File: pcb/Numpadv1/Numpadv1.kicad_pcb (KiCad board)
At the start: 2 copper layers, 104.8 x 100 mm, 37 parts, among them J1 OLED_128x32, SW1 RotaryEncoder_Switch, U1 RP2040_Zero

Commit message: PCB Completed (for now)
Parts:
- added H1: ~, ScottoKeebs_Scotto:Standoff_M2x4mm, B.Cu at (83.2, 67.3)
- added H2: ~, ScottoKeebs_Scotto:Standoff_M2x4mm, B.Cu at (83.2, 124.5)
- added H3: ~, ScottoKeebs_Scotto:Standoff_M2x4mm, B.Cu at (140.3, 105.4)
- added SW2: Switch, ScottoKeebs_Stabilizer:Stabilizer_MX_2.00u, F.Cu at (83.2, 134.0)
- added SW3: Switch, ScottoKeebs_Stabilizer:Stabilizer_MX_2.00u, F.Cu at (130.8, 124.5)
- added SW4: Switch, ScottoKeebs_Stabilizer:Stabilizer_MX_2.00u, F.Cu at (130.8, 86.4)
- S1, S10, S11, S12, S13, S14, S15, S2, S3, S4, S6, S7, S8, S9: footprint ScottoKeebs_MX:MX_PCB_1.00u -> ScottoKeebs_Hotswap:Hotswap_MX_1.00u
- S16, S17: footprint Button_Switch_Keyboard:SW_Cherry_MX_2.00u_Vertical_PCB -> ScottoKeebs_Hotswap:Hotswap_MX_2.00u_90deg
- S5: footprint Button_Switch_Keyboard:SW_Cherry_MX_2.00u_PCB -> ScottoKeebs_Hotswap:Hotswap_MX_2.00u
- moved SW1 45.1 mm to (153.5, 85.0)
- moved J1 21.4 mm to (159.4, 99.0)
- moved D13 8.57 mm to (121.3, 109.2)
- moved D11 8.57 mm to (121.3, 71.1)
- moved S5 5.68 mm to (83.2, 134.0)
- moved S16 5.68 mm to (130.8, 86.4)
- moved S17 5.68 mm to (130.8, 124.5)
- moved D12 3.81 mm to (121.3, 94.9)
- moved D14 3.81 mm to (121.3, 133.0)
- moved U1 1.91 mm to (154.1, 60.2)
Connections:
- D16 pad 1: /Row 1 -> /Row 2
- D17 pad 1: /Row 3 -> /Row 4
- S16 pad 1: Net-(D16-A) -> /Col 3
- S16 pad 2: /Col 3 -> Net-(D16-A)
- S17 pad 1: Net-(D17-A) -> /Col 3
- S17 pad 2: /Col 3 -> Net-(D17-A)
- S5 pad 1: Net-(D5-A) -> /Col 0
- S5 pad 2: /Col 0 -> Net-(D5-A)
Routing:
- net /Col 0: track 0.00 -> 186.8 mm
- net /Col 1: track 0.00 -> 143.5 mm
- net /Col 2: track 0.00 -> 143.4 mm
- net /Row 4: track 0.00 -> 120.1 mm
- net /Col 3: track 0.00 -> 117.5 mm, vias 0 -> 2
- net /Row 3: track 0.00 -> 112.9 mm
- net /Row 2: track 0.00 -> 104.1 mm
- net /Row 1: track 0.00 -> 91.7 mm
- net /Row 0: track 0.00 -> 82.9 mm
- net /GND: track 0.00 -> 66.6 mm
- net /3V3: track 0.00 -> 47.9 mm
- net /I2C0 SCL: track 0.00 -> 32.2 mm
- net /I2C0 SDA: track 0.00 -> 31.6 mm
- net /GP10: track 0.00 -> 19.0 mm
- net /GP11: track 0.00 -> 14.0 mm
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- added copper zone on B.Cu, net (none)
- added copper zone on F.Cu, net (none)

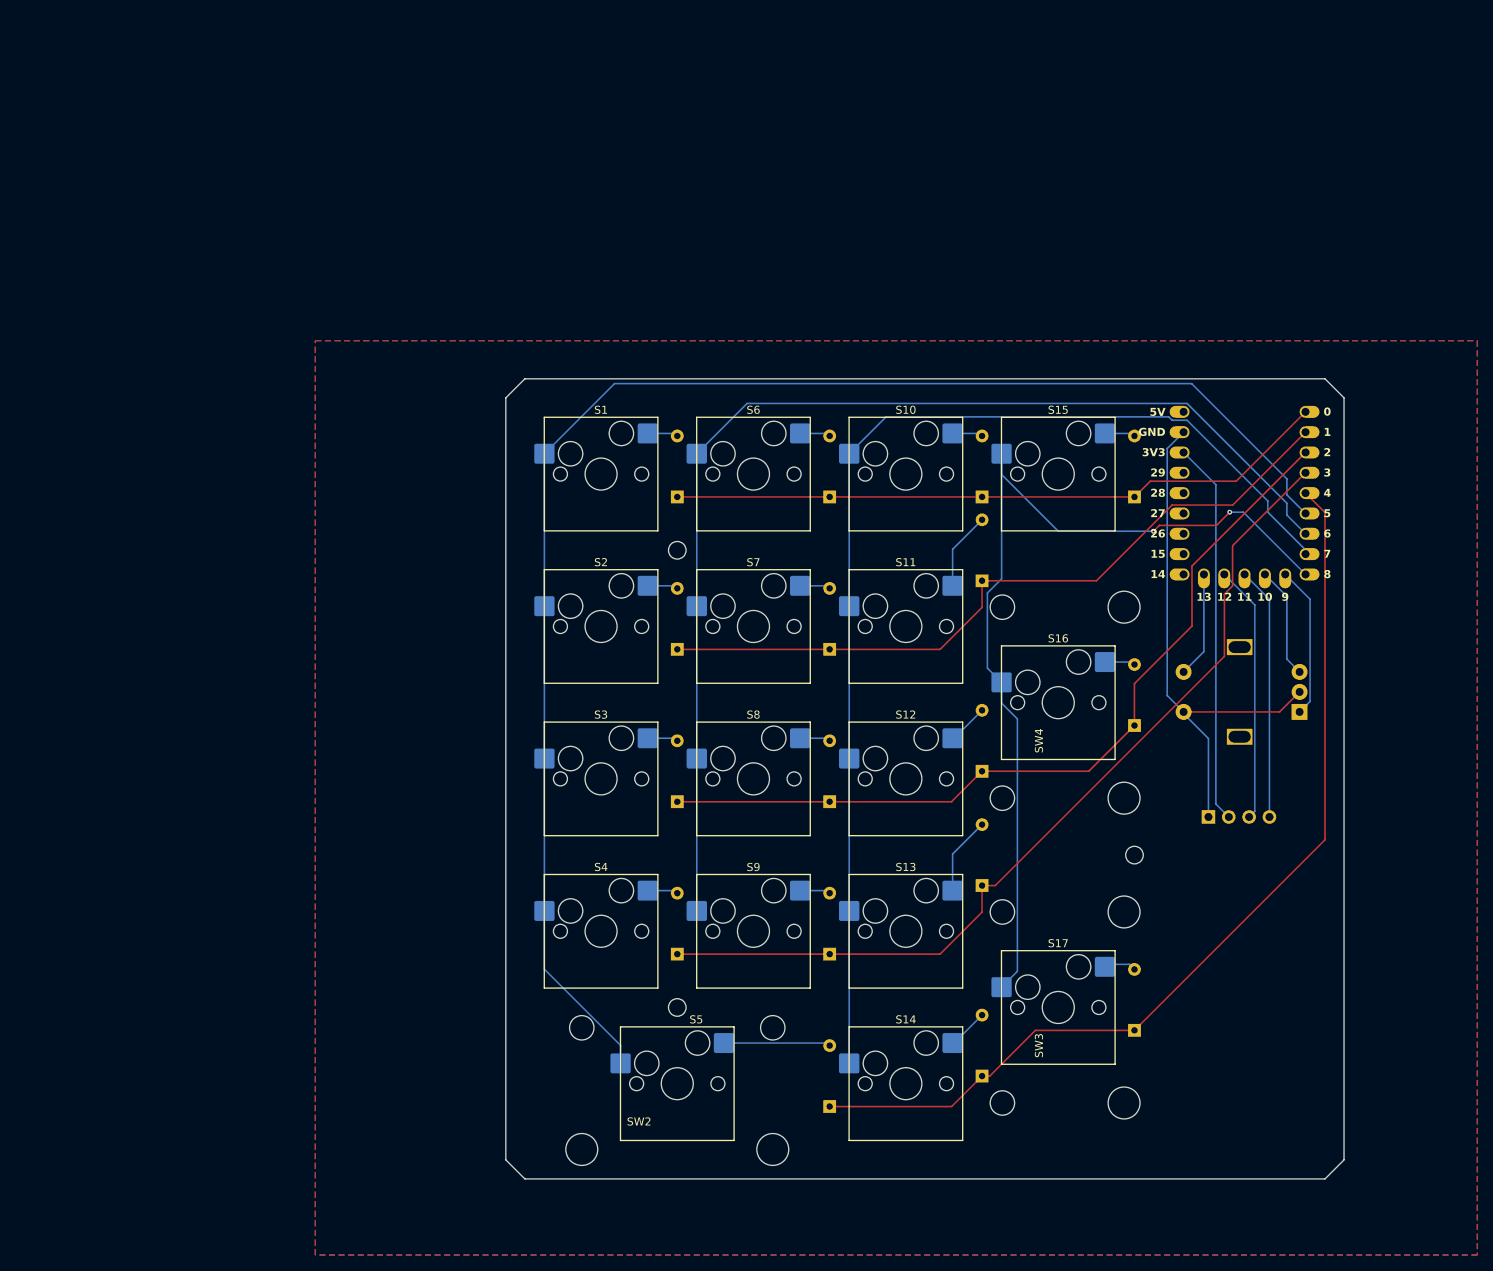
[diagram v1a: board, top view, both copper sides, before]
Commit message: Filled Zones
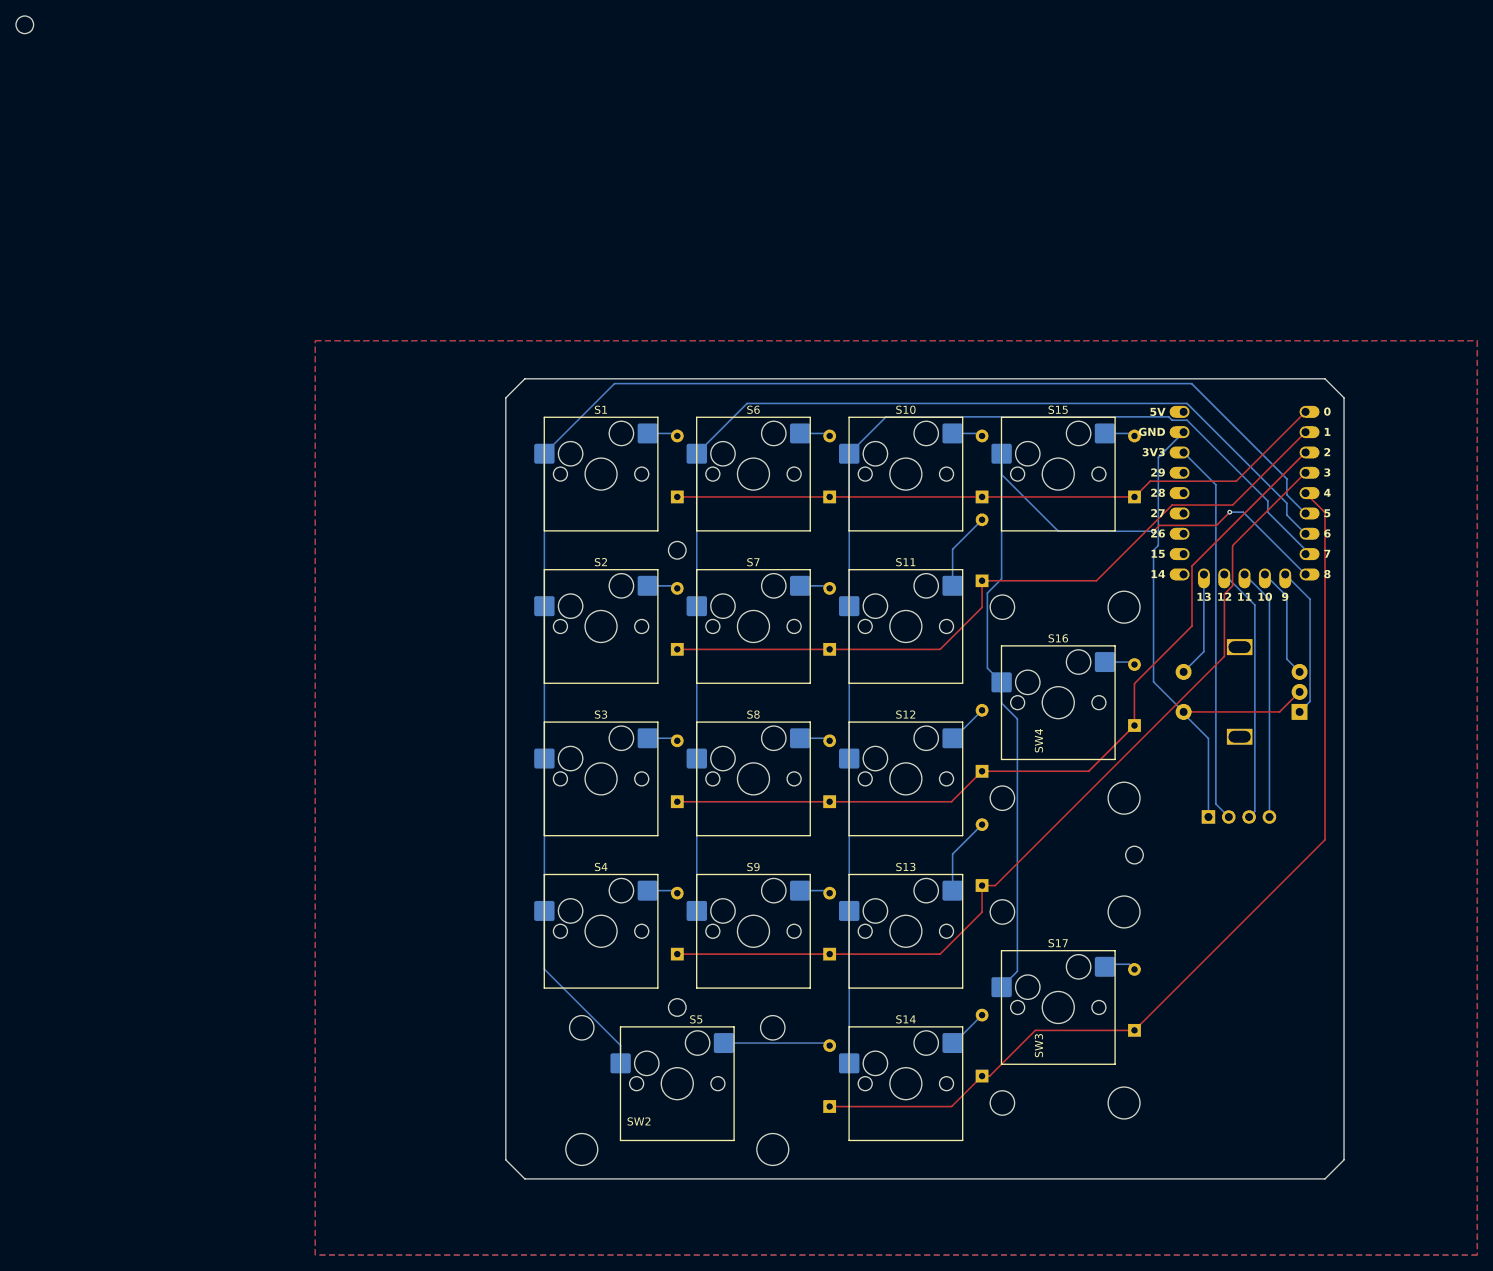
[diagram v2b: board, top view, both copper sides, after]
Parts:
- added H4: ~, ScottoKeebs_Scotto:Standoff_M2x4mm, F.Cu at (1.62, 1.62)
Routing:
- net /GND: track 66.6 -> 68.0 mm
- added copper zone on B.Cu, net /GND
- added copper zone on F.Cu, net /GND
- removed copper zone on B.Cu, net (none)
- removed copper zone on F.Cu, net (none)
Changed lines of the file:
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@@
 		)
 	)
+	(footprint "ScottoKeebs_Scotto:Standoff_M2x4mm"
+		(layer "F.Cu")
+		(at 1.625 1.625)
+		(descr "Mounting Hole 2.2mm, no annular, M2")
+		(tags "mounting hole 2.2mm no annular m2")
+		(property "Reference" "H4"
+			(at 0 -3.2 0)
+			(layer "F.SilkS")
+			(hide yes)
+			(effects
+				(font
+					(size 1 1)
+					(thickness 0.15)
+				)
+			)
+		)
+		(property "Value" "~"
+			(at 0 3.2 0)
+			(layer "F.Fab")
+			(hide yes)
+			(effects
+				(font
+					(size 1 1)
+					(thickness 0.15)
+				)
+			)
+		)
+		(property "Datasheet" ""
+			(at 0 0 0)
+			(unlocked yes)
+			(layer "F.Fab")
+			(hide yes)
+			(effects
+				(font
+					(size 1.27 1.27)
+				)
+			)
+		)
+		(property "Description" ""
+			(at 0 0 0)
+			(unlocked yes)
+			(layer "F.Fab")
+			(hide yes)
+			(effects
+				(font
+					(size 1.27 1.27)
+				)
+			)
+		)
+		(property ki_fp_filters "MountingHole*")
+		(sheetname "/")
+		(sheetfile "Numpadv1.kicad_sch")
+		(units
+			(unit
+				(name "A")
+				(pins)
+			)
+		)
+		(duplicate_pad_numbers_are_jumpers no)
+		(fp_circle
+			(center 0 0)
+			(end 1.6 0)
+			(stroke
+				(width 0.05)
+				(type default)
+			)
+			(fill no)
+			(layer "B.CrtYd")
+		)
+		(pad "" np_thru_hole circle
+			(at 0 0)
+			(size 2.2 2.2)
+			(drill 2.2)
+			(layers "*.Cu" "*.Mask")
+		)
+		(embedded_fonts no)
+		(model "${SCOTTOKEEBS_KICAD}/3dmodels/ScottoKeebs_Scotto.3dshapes/Standoff.step"
+			(offset
+				(xyz 0 0 -5.6)
+			)
+			(scale
+				(xyz 1 1 4)
+			)
+			(rotate
+				(xyz 0 0 0)
+			)
+		)
+	)
 	(footprint "ScottoKeebs_Hotswap:Hotswap_MX_1.00u"
 		(layer "F.Cu")
@@
 	)
 	(segment
-		(start 144.4275 85.465)
-		(end 146.47875 87.51625)
+		(start 142.71625 83.75375)
+		(end 142.71625 67.31)
 		(width 0.2)
 		(layer "B.Cu")
@@
 	)
 	(segment
-		(start 144.4275 54.59625)
-		(end 144.4275 85.465)
+		(start 143.31625 66.71)
+		(end 143.31625 55.7075)
+		(width 0.2)
+		(layer "B.Cu")
+		(net "/GND")
+	)
+	(segment
+		(start 142.71625 67.31)
+		(end 143.31625 66.71)
+		(width 0.2)
+		(layer "B.Cu")
+		(net "/GND")
+	)
+	(segment
+		(start 146.47875 87.51625)
+		(end 142.71625 83.75375)
 		(width 0.2)
 		(layer "B.Cu")
@@
 	)
 	(segment
-		(start 146.4775 52.54625)
-		(end 144.4275 54.59625)
+		(start 143.31625 55.7075)
+		(end 146.4775 52.54625)
 		(width 0.2)
 		(layer "B.Cu")
@@
 	)
 	(zone
+		(net "/GND")
 		(layers "F.Cu" "B.Cu")
 		(hatch edge 0.5)
@@
 			(thermal_gap 0.5)
 			(thermal_bridge_width 0.5)
-			(island_removal_mode 1)
+			(island_removal_mode 0)
 		)
 		(polygon

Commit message: PCB Manufacturing Files
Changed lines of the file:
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@@
 			(plot_on_all_layers_selection 0x00000000_00000000_00000000_00000000)
 			(disableapertmacros no)
-			(usegerberextensions no)
+			(usegerberextensions yes)
 			(usegerberattributes yes)
 			(usegerberadvancedattributes yes)
@@
 			(outputformat 1)
 			(mirror no)
-			(drillshape 1)
+			(drillshape 0)
 			(scaleselection 1)
-			(outputdirectory "")
+			(outputdirectory "../Fabrication/")
 		)
 	)
@@
 	(footprint "ScottoKeebs_Stabilizer:Stabilizer_MX_2.00u"
 		(layer "F.Cu")
-		(at 130.81 124.46 90)
+		(at 130.81 124.49175 90)
 		(descr "MX PCB Stabilizer 2.00u 2.25u 2.50u 2.75u")
 		(tags "MX Keyboard Stabilizer 2.00u 2.25u 2.50u 2.75u Cutout")
